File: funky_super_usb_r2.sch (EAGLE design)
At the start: 28 parts, among them IC1 TINY24/44/84-SSU, IC2 LTC3525, IC3 MCP1703CB, X1 USB-MICROB

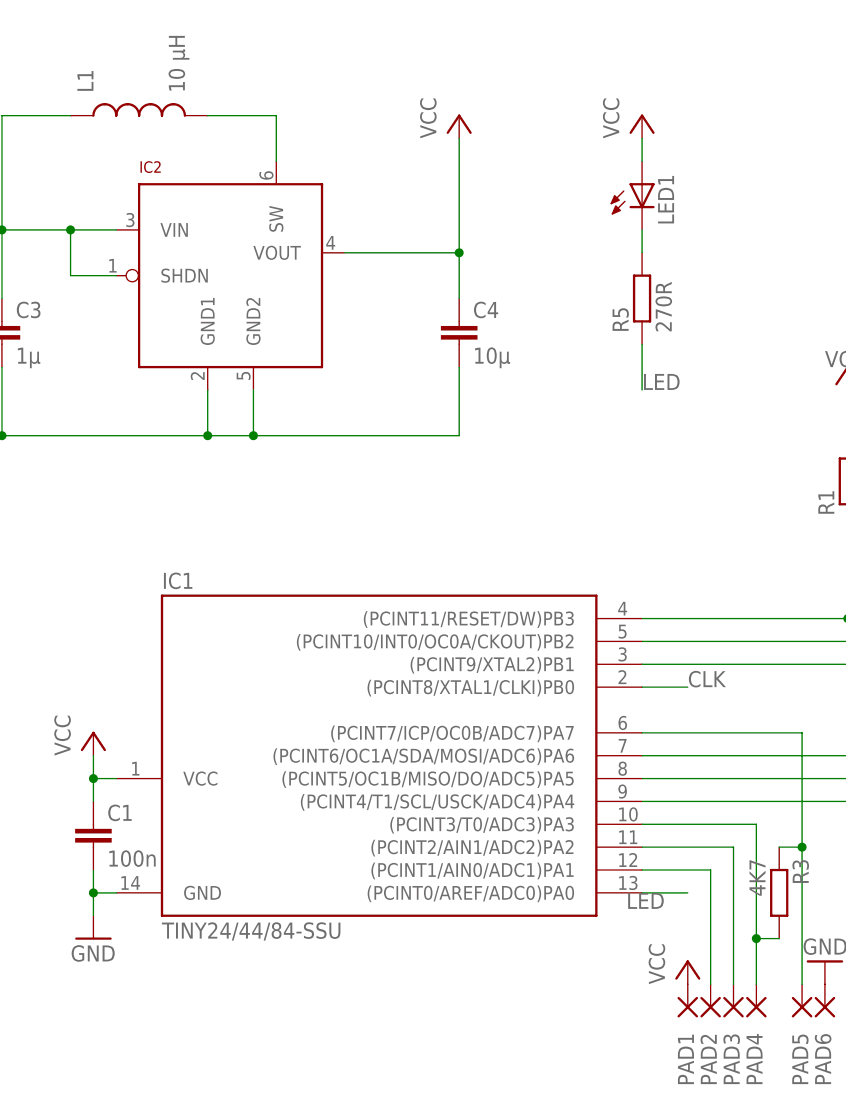
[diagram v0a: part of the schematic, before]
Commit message: edited silk and reduced vias
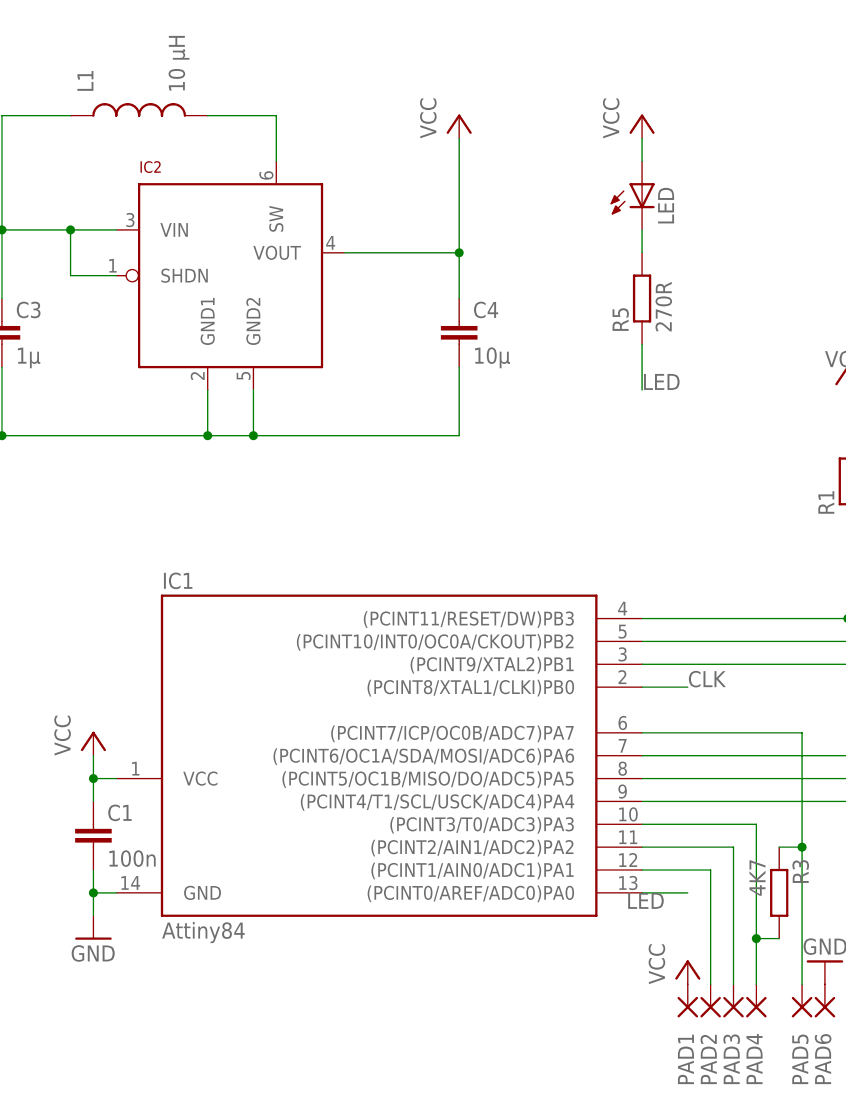
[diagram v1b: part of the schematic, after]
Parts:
- IC1: value TINY24/44/84-SSU -> Attiny84
- renumbered LED1 to LED, U$1 to RFM12B
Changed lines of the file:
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@@
 </classes>
 <parts>
-<part name="U$1" library="JeeParts" deviceset="RFM12B" device=""/>
-<part name="IC1" library="avr-7" deviceset="TINY24/44/84" device="-SSU"/>
+<part name="RFM12B" library="JeeParts" deviceset="RFM12B" device=""/>
+<part name="IC1" library="avr-7" deviceset="TINY24/44/84" device="-SSU" value="Attiny84"/>
 <part name="C1" library="rcl" deviceset="C-EU" device="C0603K" value="100n"/>
 <part name="R1" library="resistor" deviceset="R-EU_" device="R0603" value="10K"/>
@@
 <part name="BAT2" library="SparkFun" deviceset="BATTERY" device="20PTH"/>
 <part name="JP2" library="SparkFun" deviceset="M01" device="PTH"/>
-<part name="LED1" library="SparkFun" deviceset="LED" device="0603"/>
+<part name="LED" library="SparkFun" deviceset="LED" device="0603"/>
 <part name="R5" library="resistor" deviceset="R-EU_" device="R0603" value="270R"/>
 <part name="P+10" library="supply1" deviceset="VCC" device=""/>
@@
 </plain>
 <instances>
-<instance part="U$1" gate="G$1" x="160.02" y="55.88"/>
+<instance part="RFM12B" gate="G$1" x="160.02" y="55.88"/>
 <instance part="IC1" gate="1" x="38.1" y="53.34"/>
 <instance part="C1" gate="G$1" x="27.94" y="45.72"/>
@@
 <instance part="BAT2" gate="G$1" x="-12.7" y="50.8" rot="R270"/>
 <instance part="JP2" gate="G$1" x="187.96" y="50.8" rot="R180"/>
-<instance part="LED1" gate="G$1" x="88.9" y="116.84"/>
+<instance part="LED" gate="G$1" x="88.9" y="116.84"/>
 <instance part="R5" gate="G$1" x="88.9" y="104.14" rot="R90"/>
 <instance part="P+10" gate="VCC" x="88.9" y="124.46"/>
@@
 </segment>
 <segment>
-<pinref part="U$1" gate="G$1" pin="VCC"/>
+<pinref part="RFM12B" gate="G$1" pin="VCC"/>
 <pinref part="P+4" gate="VCC" pin="VCC"/>
 <wire x1="160.02" y1="71.12" x2="160.02" y2="68.58" width="0.1524" layer="91"/>
@@
 </segment>
 <segment>
-<pinref part="LED1" gate="G$1" pin="A"/>
+<pinref part="LED" gate="G$1" pin="A"/>
 <pinref part="P+10" gate="VCC" pin="VCC"/>
 <wire x1="88.9" y1="119.38" x2="88.9" y2="121.92" width="0.1524" layer="91"/>
@@
 </segment>
 <segment>
-<pinref part="U$1" gate="G$1" pin="GND"/>
+<pinref part="RFM12B" gate="G$1" pin="GND"/>
 <pinref part="GND2" gate="1" pin="GND"/>
 <wire x1="160.02" y1="35.56" x2="160.02" y2="40.64" width="0.1524" layer="91"/>
@@
 <wire x1="88.9" y1="63.5" x2="116.84" y2="63.5" width="0.1524" layer="91"/>
 <wire x1="116.84" y1="63.5" x2="116.84" y2="78.74" width="0.1524" layer="91"/>
-<pinref part="U$1" gate="G$1" pin="SEL"/>
+<pinref part="RFM12B" gate="G$1" pin="SEL"/>
 <wire x1="147.32" y1="60.96" x2="116.84" y2="60.96" width="0.1524" layer="91"/>
 <wire x1="116.84" y1="60.96" x2="116.84" y2="63.5" width="0.1524" layer="91"/>
@@
 <wire x1="88.9" y1="48.26" x2="114.3" y2="48.26" width="0.1524" layer="91"/>
 <wire x1="114.3" y1="48.26" x2="114.3" y2="58.42" width="0.1524" layer="91"/>
-<pinref part="U$1" gate="G$1" pin="SCK"/>
+<pinref part="RFM12B" gate="G$1" pin="SCK"/>
 <wire x1="114.3" y1="58.42" x2="147.32" y2="58.42" width="0.1524" layer="91"/>
 <pinref part="U$2" gate="G$1" pin="P$2"/>
@@
 <net name="N$5" class="0">
 <segment>
-<pinref part="U$1" gate="G$1" pin="SDI"/>
+<pinref part="RFM12B" gate="G$1" pin="SDI"/>
 <wire x1="147.32" y1="55.88" x2="119.38" y2="55.88" width="0.1524" layer="91"/>
 <wire x1="119.38" y1="55.88" x2="119.38" y2="50.8" width="0.1524" layer="91"/>
@@
 <segment>
 <pinref part="IC1" gate="1" pin="(PCINT6/OC1A/SDA/MOSI/ADC6)PA6"/>
-<pinref part="U$1" gate="G$1" pin="SDO"/>
+<pinref part="RFM12B" gate="G$1" pin="SDO"/>
 <wire x1="88.9" y1="53.34" x2="139.7" y2="53.34" width="0.1524" layer="91"/>
 <pinref part="U$2" gate="G$1" pin="P$5"/>
@@
 <wire x1="88.9" y1="66.04" x2="132.08" y2="66.04" width="0.1524" layer="91"/>
 <wire x1="132.08" y1="66.04" x2="132.08" y2="48.26" width="0.1524" layer="91"/>
-<pinref part="U$1" gate="G$1" pin="IRQ"/>
+<pinref part="RFM12B" gate="G$1" pin="IRQ"/>
 <wire x1="132.08" y1="48.26" x2="147.32" y2="48.26" width="0.1524" layer="91"/>
 </segment>
@@
 <net name="N$3" class="0">
 <segment>
-<pinref part="U$1" gate="G$1" pin="ANT"/>
+<pinref part="RFM12B" gate="G$1" pin="ANT"/>
 <wire x1="172.72" y1="50.8" x2="180.34" y2="50.8" width="0.1524" layer="91"/>
 <pinref part="JP2" gate="G$1" pin="1"/>
@@
 <segment>
 <pinref part="R5" gate="G$1" pin="2"/>
-<pinref part="LED1" gate="G$1" pin="C"/>
+<pinref part="LED" gate="G$1" pin="C"/>
 <wire x1="88.9" y1="109.22" x2="88.9" y2="111.76" width="0.1524" layer="91"/>
 </segment>
@@
 </segment>
 <segment>
-<pinref part="U$1" gate="G$1" pin="CLK"/>
+<pinref part="RFM12B" gate="G$1" pin="CLK"/>
 <wire x1="147.32" y1="50.8" x2="142.24" y2="50.8" width="0.1524" layer="91"/>
 </segment>
